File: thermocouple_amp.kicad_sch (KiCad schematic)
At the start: 0 parts

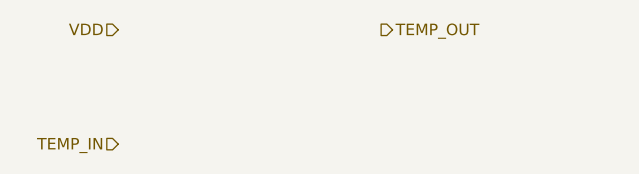
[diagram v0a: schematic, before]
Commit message: Added discharge Mosfet.
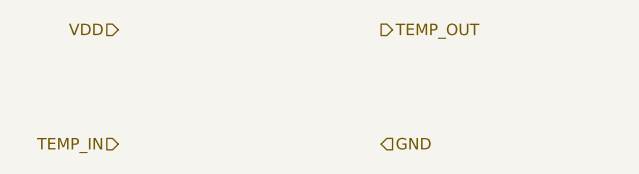
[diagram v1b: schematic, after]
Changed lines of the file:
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@@
+		)
+	)
+	(hierarchical_label "GND"
+		(shape input)
+		(at 52.07 33.02 0)
+		(fields_autoplaced yes)
+		(effects
+			(font
+				(size 1.27 1.27)
+			)
+			(justify left)
 		)
 	)

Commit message: Prepared STS1_BATT_TEST.
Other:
- note added: "Choose a suitable amplifier for the thermocouple here. You got 5V supply voltage (VDD) from the Labjack here that can be used to power the amplifier."
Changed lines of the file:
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@@
 	(generator_version "8.0")
 	(paper "A4")
+	(text "Choose a suitable amplifier for the thermocouple here. \nYou got 5V supply voltage (VDD) from the Labjack here\nthat can be used to power the amplifier."
+		(exclude_from_sim no)
+		(at 45.72 26.416 0)
+		(effects
+			(font
+				(size 1.27 1.27)
+			)
+		)
+	)
 	(hierarchical_label "TEMP_IN"
 		(shape input)
